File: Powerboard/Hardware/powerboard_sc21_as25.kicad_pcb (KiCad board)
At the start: 4 copper layers, 86.3 x 55.6 mm, 150 parts, among them IC1 BQ24618RGET-iclr, IC2 CP2102, J1 Thermistor Connection 103AT N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, J10 Conn_01x04_Male, J11 Conn_01x03_MountingPin, J2 Conn_01x02_Male, J3 Conn_01x02_Male, J4 Conn_01x08_Male, J5 Conn_01x04_Male, J6 Conn_01x02_Male, J7 IsolationSwitch, J8 USB_C_Receptacle_USB2.0, J9 Conn_Coaxial, Q1 RSJ250P10TL, Q10 MCH6351, Q2 RSJ250P10TL, Q3 RSJ250P10TL, Q4 RS1G120MN, Q5 RS1G120MN, Q6 MMDT2222A, Q7 RSJ250P10TL, Q8 RSJ250P10TL, Q9 MCH6351, U1 LTC4412xS6, U11 LTC4411, U2 SN65HVD230, U3 ESP32-PICO-D4, U4 SC4216H, U6 LM2679T-3.3-iclr, U7 LM2679T-3.3-iclr, U8 LTC4412xS6, U9 LTC4412xS6

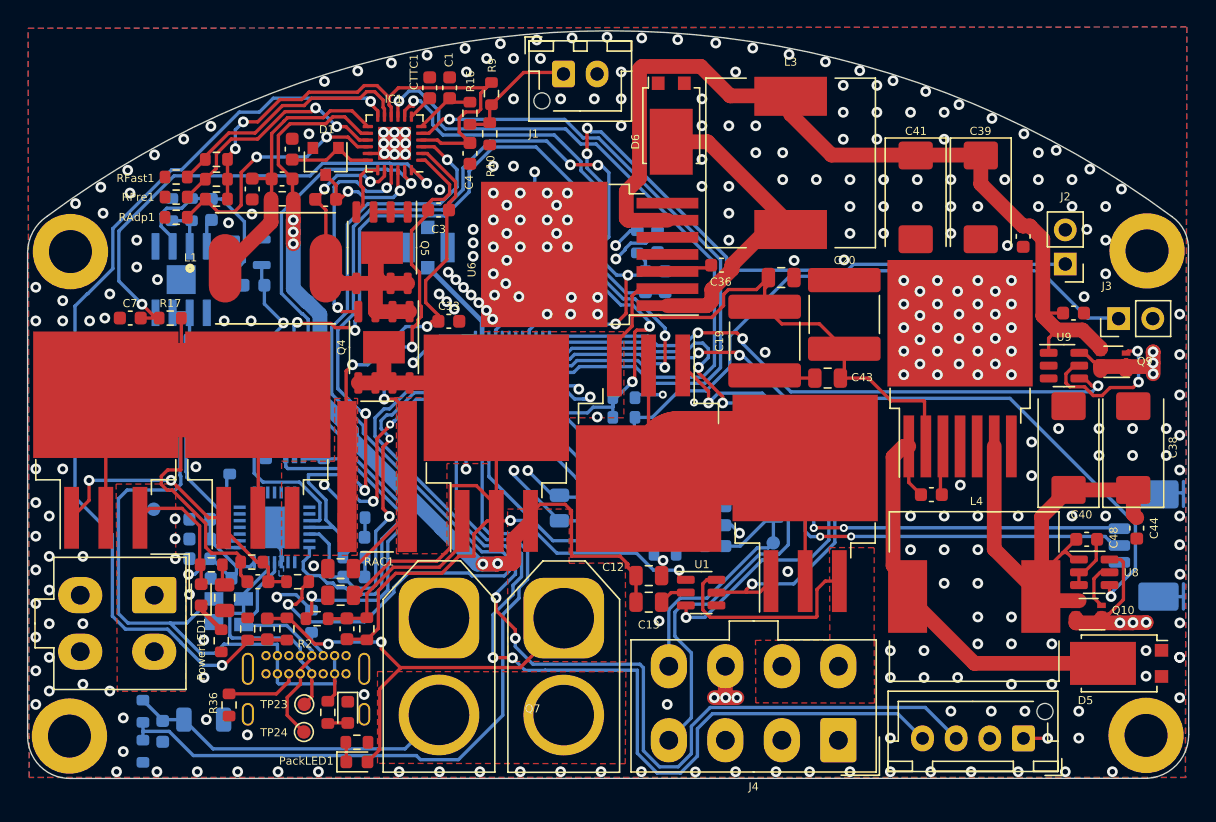
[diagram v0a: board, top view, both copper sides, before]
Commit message: Fixed file location and changed a trace width
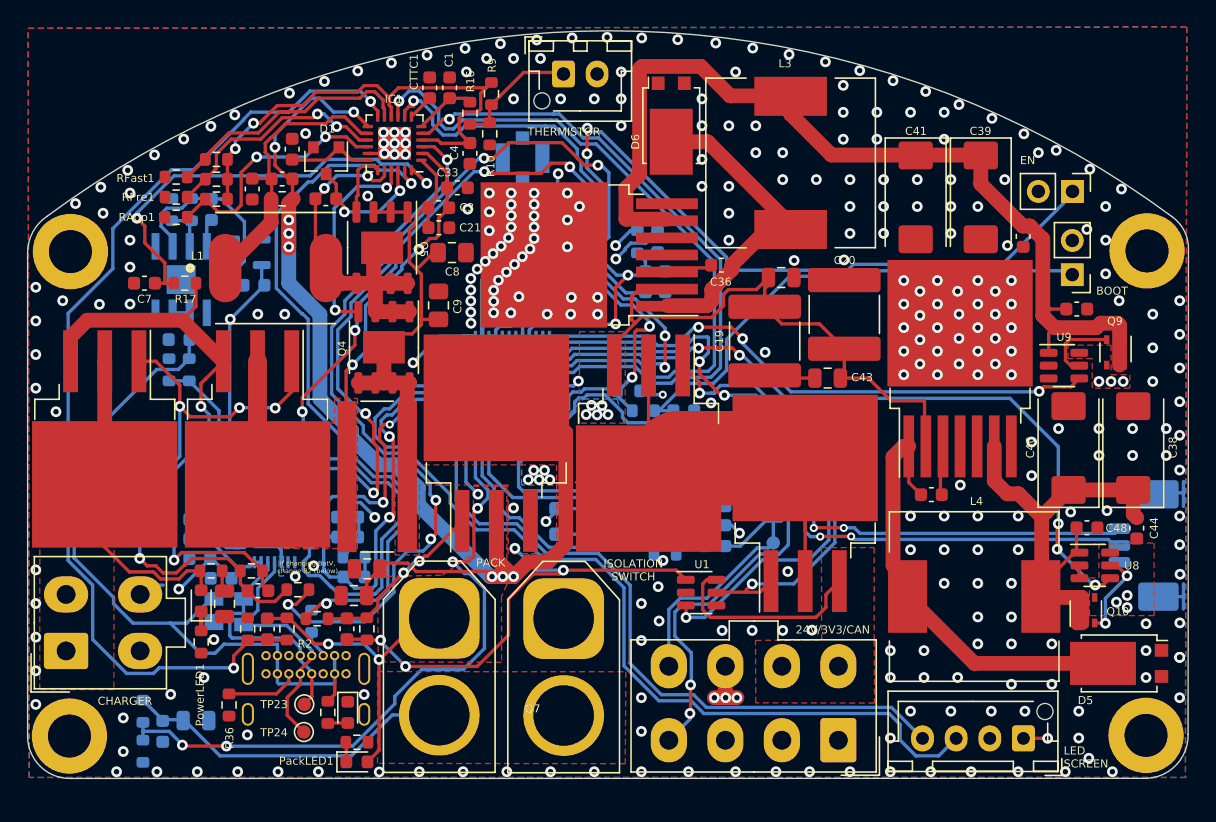
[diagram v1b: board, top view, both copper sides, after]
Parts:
- added C21: 0.1uF, Capacitor_SMD:C_0603_1608Metric, F.Cu at (79.5, 42.1)
- C32: value 22uF -> 10uF; footprint Capacitor_SMD:C_1206_3216Metric -> Capacitor_SMD:C_0805_2012Metric
- C8, C9: footprint Capacitor_SMD:C_0805_2012Metric -> Capacitor_SMD:C_0805_2012Metric_Pad1.18x1.45mm_HandSolder
- R10: value 430k -> 10.5k
- R9: value 9.31k -> 2.7k
- moved C8 24.9 mm to (80.4, 43.9)
- moved C9 22.7 mm to (79.4, 47.9), turned to 90 degrees
- moved C12 22.0 mm to (73.1, 69.4)
- moved C13 21.1 mm to (74.1, 67.4)
- moved C33 9.94 mm to (80.8, 39.1)
- moved J9 9.68 mm to (85.7, 36.9)
- moved J6 9.27 mm to (88.7, 71.1)
- moved J7 9.25 mm to (79.5, 71.1)
- moved J5 7.75 mm to (51.8, 73.5), turned to 90 degrees
- moved J2 5.42 mm to (126.5, 39.4), turned to -90 degrees
- moved C18 4.86 mm to (97.7, 55.7), turned to 180 degrees
- moved J3 4.74 mm to (126.5, 45.6), turned to 180 degrees
- moved R17 2.81 mm to (60.6, 46.2)
- moved C7 2.80 mm to (57.6, 46.2)
- moved R8 1.53 mm to (94.7, 55.7)
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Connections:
- C11 pad 1: /Battery Charger/Q3-S -> /Battery Charger/SRP
- C11 pad 2: /Battery Charger/SRP -> /Battery Charger/Q3-D
- C12 pad 1: GND -> /Battery Charger/Q3-D
- C12 pad 2: /Battery Charger/Q3-S -> GND
- C13 pad 1: GND -> /Battery Charger/Q3-D
- C13 pad 2: /Battery Charger/Q3-S -> GND
- C14 pad 1: /Battery Charger/Q1-D -> /Battery Charger/Q1-S
- C16 pad 1: GND -> Net-(C16-Pad1)
- C16 pad 2: Net-(C16-Pad2) -> GND
- C8 pad 1: GND -> +24V
- C8 pad 2: +24V -> GND
- C9 pad 1: GND -> +24V
- C9 pad 2: +24V -> GND
- Cff1 pad 2: /Battery Charger/Q3-S -> /Battery Charger/Q3-D
- IC1 pad 13: /Battery Charger/SRP -> /Battery Charger/Q3-D
- IC1 pad 14: /Battery Charger/Q3-S -> /Battery Charger/SRP
- J7 pad 1: /Battery Charger/Q3-S -> /Battery Charger/Q3-D
- PackLED1 pad 2: /Battery Charger/Q3-S -> /Battery Charger/Q3-D
- Q1 pad 2: /Battery Charger/Q1-D -> Net-(J5-Pad1)
- Q1 pad 3: Net-(J5-Pad1) -> /Battery Charger/Q1-S
- Q10 pad 1: +3V3 -> Net-(C38-Pad1)
- Q10 pad 2: +3V3 -> Net-(C38-Pad1)
- Q10 pad 4: Net-(C38-Pad1) -> +3V3
- Q10 pad 5: +3V3 -> Net-(C38-Pad1)
- Q10 pad 6: +3V3 -> Net-(C38-Pad1)
- Q2 pad 2: /Battery Charger/Q1-D -> Net-(C3-Pad1)
- Q2 pad 3: Net-(C3-Pad1) -> /Battery Charger/Q1-S
- Q3 pad 2: +24V -> /Battery Charger/Q3-D
- Q3 pad 3: /Battery Charger/Q3-S -> +24V
- Q9 pad 1: +3V3 -> Net-(C39-Pad1)
- Q9 pad 2: +3V3 -> Net-(C39-Pad1)
- Q9 pad 4: Net-(C39-Pad1) -> +3V3
- Q9 pad 5: +3V3 -> Net-(C39-Pad1)
- Q9 pad 6: +3V3 -> Net-(C39-Pad1)
- R14 pad 1: /Battery Charger/Q1-D -> /Battery Charger/Q1-S
- R17 pad 2: /Battery Charger/Q1-D -> /Battery Charger/Q1-S
- R2 pad 2: /Battery Charger/Q3-S -> /Battery Charger/Q3-D
- R20 pad 1: Net-(C16-Pad2) -> Net-(C16-Pad1)
- RSR1 pad 1: /Battery Charger/Q3-S -> /Battery Charger/Q3-D
- U3 pad 20: GND -> unconnected-(U3-Pad20)
- U3 pad 25: /PDU_EN -> unconnected-(U3-Pad25)
- U3 pad 27: /CAN_RX -> unconnected-(U3-Pad27)
- U3 pad 28: unconnected-(U3-Pad28) -> /PDU_EN
- U3 pad 34: /CAN_TX -> /CAN_RX
- U3 pad 35: /CHARGE -> /CAN_TX
- U3 pad 36: unconnected-(U3-Pad36) -> /CHARGE
- U3 pad 8: unconnected-(U3-Pad8) -> GND
- U6 pad 5: unconnected-(U6-Pad5) -> GND
- U7 pad 5: unconnected-(U7-Pad5) -> GND
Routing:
- net /Battery Charger/Q3-D: track 0.00 -> 115.9 mm, vias 0 -> 10
- net /Battery Charger/Q3-S: track 103.7 -> 0.00 mm, vias 7 -> 0
- net /Battery Charger/Q1-D: track 54.7 -> 0.00 mm
- net /Battery Charger/Q1-S: track 0.00 -> 43.9 mm, vias 0 -> 2
- net +24V: track 156.1 -> 116.4 mm, vias 4 -> 14
- net /Battery Charger/Q1-G: track 22.2 -> 43.6 mm, vias 2 -> 4
- net +3V3: track 101.6 -> 84.2 mm
- net GND: track 58.1 -> 43.1 mm, vias 310 -> 302
- net /SCL: track 65.9 -> 53.0 mm, vias 2 -> 0
- net Net-(IC1-Pad3): track 68.2 -> 55.3 mm, vias 2 -> 4
- net Net-(J5-Pad1): track 10.9 -> 21.9 mm
- net /SDA: track 75.2 -> 67.1 mm, vias 2 -> 0
- net Net-(C18-Pad2): track 45.4 -> 38.2 mm
- net /PDU_EN: track 50.1 -> 57.1 mm
- net /BOOT: track 68.0 -> 61.5 mm, vias 4 -> 6
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- added copper zone on B.Cu, net +24V
- added copper zone on F.Cu, net +3V3
- added copper zone on F.Cu, net /Battery Charger/Q3-D
- removed copper zone on F.Cu, net /Battery Charger/Q3-S
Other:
- outline, holes or cut-outs redrawn
- board text added: "24V/3V3/CAN"
- board text added: "BOOT"
- board text added: "CHARGER"
- board text added: "EN"
- board text added: "ISOLATION SWITCH"
- board text added: "If changing BatV, change R2 (below)"
- board text added: "LED SCREEN"
- board text added: "PACK"
- board text added: "PDU ENABLE"
- board text added: "RF CONN"
- board text added: "THERMISTOR"

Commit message: Added PCB name on back silkscreen + version numbering
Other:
- board text added: "Lightning McQueen"
- board text added: "v1"
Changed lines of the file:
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@@
   (gr_arc (start 50.32 41.24) (mid 92.115 27.444209) (end 133.91 41.24) (layer "Edge.Cuts") (width 0.1))
   (gr_line (start 52.05 83) (end 132.08 82.99) (layer "Edge.Cuts") (width 0.1))
+  (gr_text "v1" (at 95.85 37.08) (layer "B.SilkS")
+    (effects (font (size 2 2) (thickness 0.3)) (justify mirror))
+  )
   (gr_text "Designed by \nKiran de Silva\nShiven Chandarana\nAndrei Paduraru\nArtem Sheykin\n" (at 117.8 63.1) (layer "B.SilkS")
     (effects (font (size 1 1) (thickness 0.15)) (justify mirror))
   )
-  (gr_text "RF CONN" (at 85.825 34) (layer "B.SilkS")
+  (gr_text "RF CONN" (at 81.83 37.24 270) (layer "B.SilkS")
     (effects (font (size 0.6 0.6) (thickness 0.1)) (justify mirror))
   )
@@
     (effects (font (size 1 1) (thickness 0.15)) (justify mirror))
   )
+  (gr_text "Lightning McQueen" (at 89.56 33.01) (layer "B.SilkS")
+    (effects (font (size 3 3) (thickness 0.5)) (justify mirror))
+  )
   (gr_text "BOOT" (at 129.475 46.775) (layer "F.SilkS")

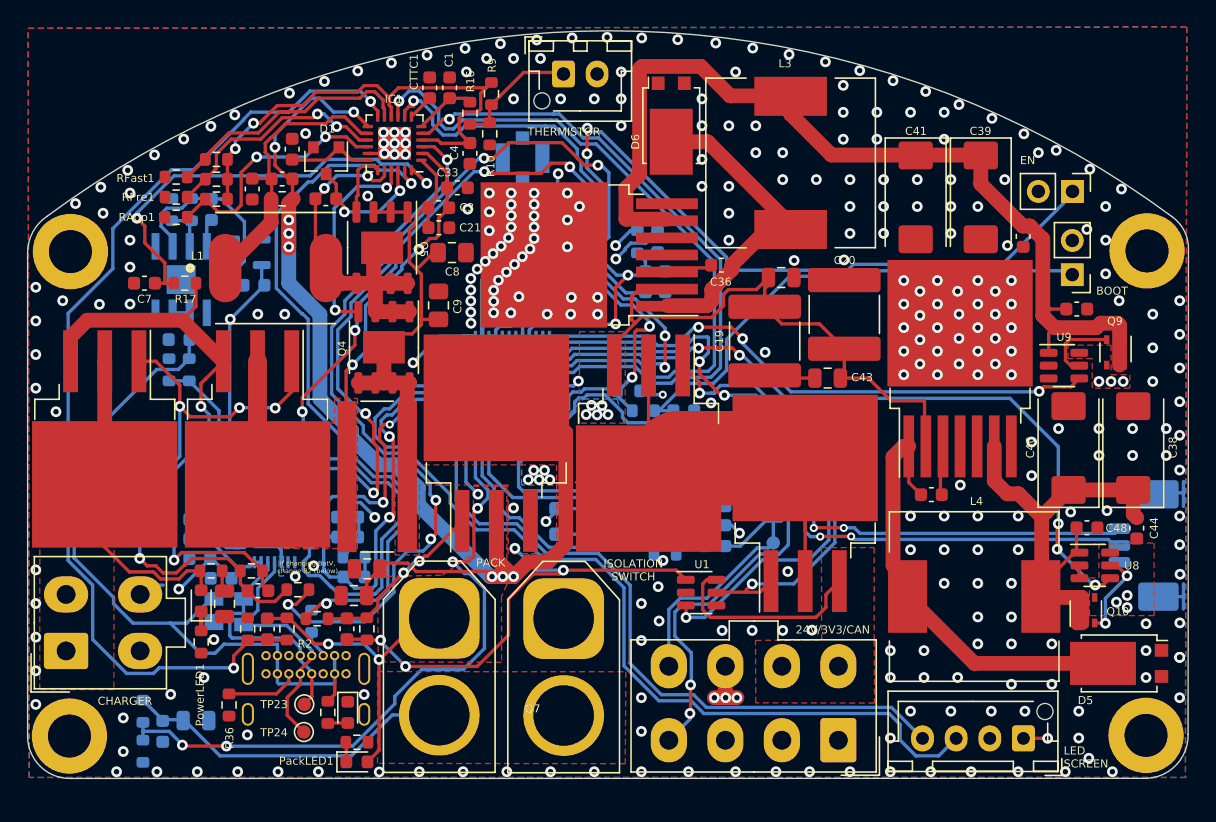
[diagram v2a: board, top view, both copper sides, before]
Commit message: did some final fixes with track width
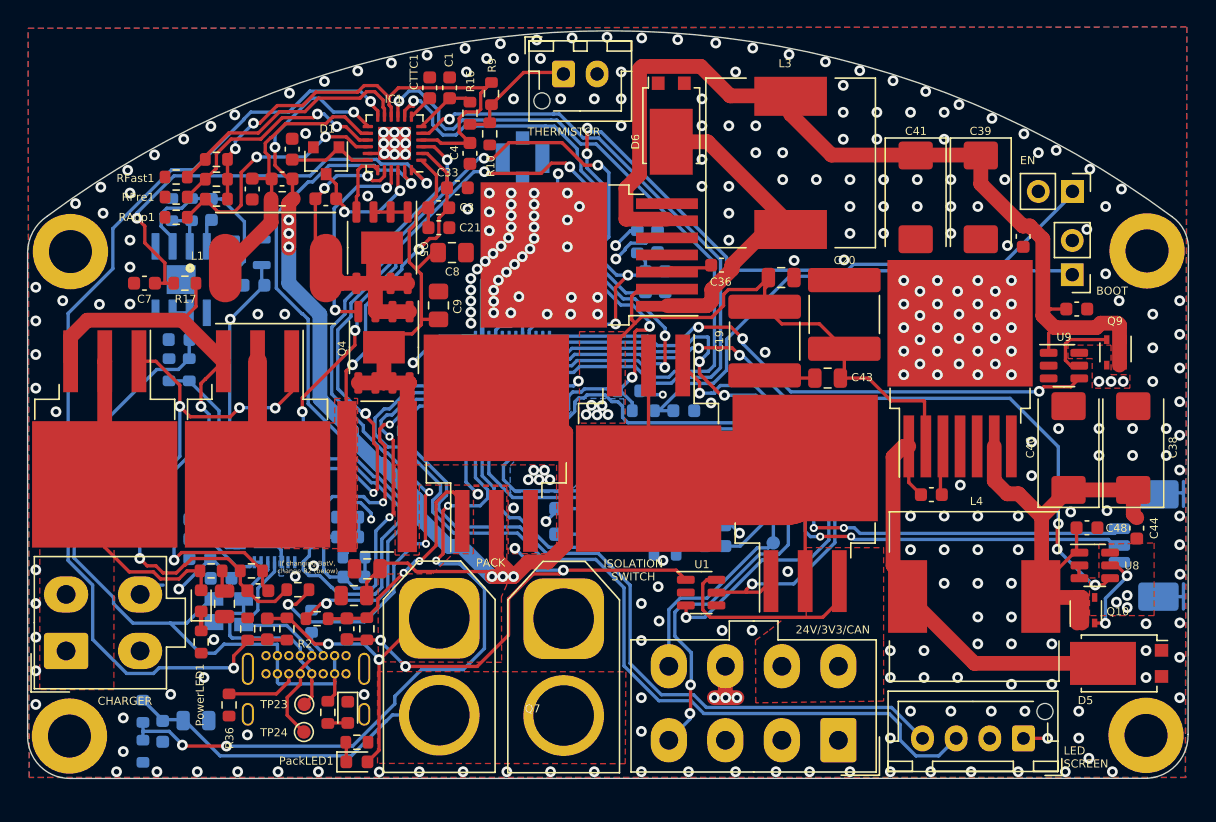
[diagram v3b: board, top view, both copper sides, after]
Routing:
- net +24V: track 116.4 -> 107.1 mm
- net GND: track 43.1 -> 35.3 mm, vias 302 -> 298
- net /Battery Charger/Q3-D: track 115.9 -> 108.7 mm
- net /SCL: track 53.0 -> 59.9 mm
- net Net-(C15-Pad2): track 13.3 -> 16.2 mm
- net /CHARGE: track 50.2 -> 52.6 mm
- net Net-(C36-Pad2): track 24.0 -> 21.9 mm
- net /Battery Charger/PH: track 26.3 -> 24.3 mm
- net /SDA: track 67.1 -> 68.7 mm
- net Net-(C37-Pad2): track 32.9 -> 31.6 mm
- net Net-(IC1-Pad3): track 55.3 -> 54.1 mm
- net Net-(J4-Pad5): track 15.1 -> 14.0 mm
- net /PDU_EN: track 57.1 -> 58.0 mm
- net /Battery Charger/CE: track 37.7 -> 36.9 mm
- net Net-(J5-Pad1): track 21.9 -> 21.1 mm
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
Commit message: changed can h and i2c lines so vias are more conssitent
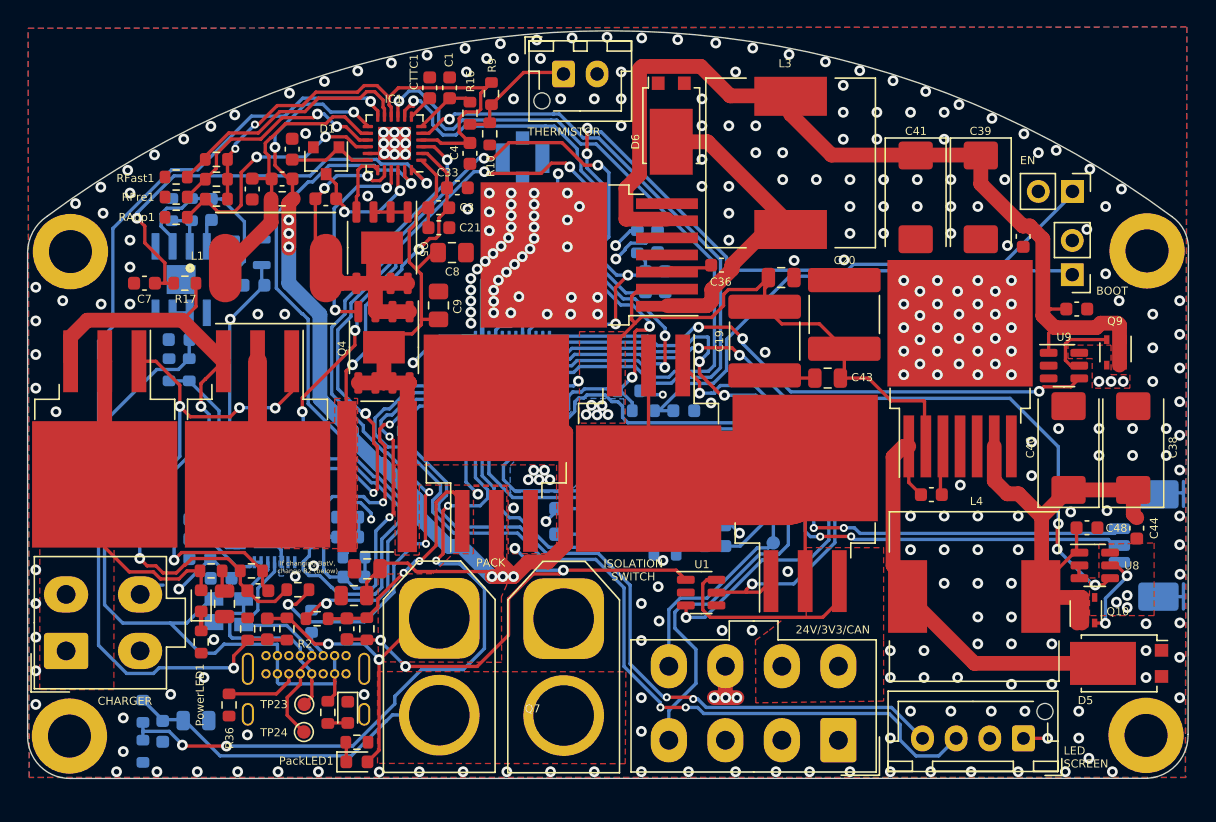
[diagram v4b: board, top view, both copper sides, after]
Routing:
- net /Battery Charger/VFB: track 74.7 -> 72.3 mm
- net VBUS: track 57.8 -> 56.4 mm
- net /CANL: track 38.2 -> 38.5 mm, vias 2 -> 0
- net /SDA: track 68.7 -> 68.9 mm, vias 0 -> 2
- net /SCL: vias 0 -> 2
